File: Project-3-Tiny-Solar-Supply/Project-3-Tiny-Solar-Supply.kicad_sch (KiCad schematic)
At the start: 16 parts, among them J1 Conn_01x02_Pin, J2 Conn_01x02_Pin, J3 Conn_01x02_Pin, J4 Conn_01x02_Pin, Q1 2N7002, U1 AP3015AKTR-G1

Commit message: assign remaining footprints to symbols
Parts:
- C1, C3: footprint (none) -> Capacitor_SMD:C_0805_2012Metric
- C2: footprint (none) -> Capacitor_SMD:C_1206_3216Metric
- J1, J2, J3: footprint (none) -> Connector_PinHeader_2.54mm:PinHeader_1x02_P2.54mm_Vertical
- J4: footprint (none) -> Connector_PinHeader_2.54mm:PinHeader_1x02_P2.54mm_Horizontal
- R1, R2, R3, R4: footprint (none) -> Resistor_SMD:R_0805_2012Metric
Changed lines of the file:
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@@
 			)
 		)
-		(property "Footprint" ""
+		(property "Footprint" "Connector_PinHeader_2.54mm:PinHeader_1x02_P2.54mm_Vertical"
 			(at 86.36 54.61 0)
 			(hide yes)
@@
 			)
 		)
-		(property "Footprint" ""
+		(property "Footprint" "Resistor_SMD:R_0805_2012Metric"
 			(at 116.332 45.72 90)
 			(hide yes)
@@
 			)
 		)
-		(property "Footprint" ""
+		(property "Footprint" "Capacitor_SMD:C_0805_2012Metric"
 			(at 216.8652 52.07 0)
 			(hide yes)
@@
 			)
 		)
-		(property "Footprint" ""
+		(property "Footprint" "Connector_PinHeader_2.54mm:PinHeader_1x02_P2.54mm_Horizontal"
 			(at 53.34 52.07 0)
 			(hide yes)
@@
 			)
 		)
-		(property "Footprint" ""
+		(property "Footprint" "Resistor_SMD:R_0805_2012Metric"
 			(at 62.992 67.31 90)
 			(hide yes)
@@
 			)
 		)
-		(property "Footprint" ""
+		(property "Footprint" "Connector_PinHeader_2.54mm:PinHeader_1x02_P2.54mm_Vertical"
 			(at 104.14 34.29 0)
 			(hide yes)
@@
 			)
 		)
-		(property "Footprint" ""
+		(property "Footprint" "Resistor_SMD:R_0805_2012Metric"
 			(at 198.882 81.28 90)
 			(hide yes)
@@
 			)
 		)
-		(property "Footprint" ""
+		(property "Footprint" "Capacitor_SMD:C_1206_3216Metric"
 			(at 224.4852 69.85 0)
 			(hide yes)
@@
 			)
 		)
-		(property "Footprint" ""
+		(property "Footprint" "Resistor_SMD:R_0805_2012Metric"
 			(at 198.882 48.26 90)
 			(hide yes)
@@
 			)
 		)
-		(property "Footprint" ""
+		(property "Footprint" "Capacitor_SMD:C_0805_2012Metric"
 			(at 135.5852 85.09 0)
 			(hide yes)
@@
 			)
 		)
-		(property "Footprint" ""
+		(property "Footprint" "Connector_PinHeader_2.54mm:PinHeader_1x02_P2.54mm_Vertical"
 			(at 240.03 59.69 0)
 			(hide yes)

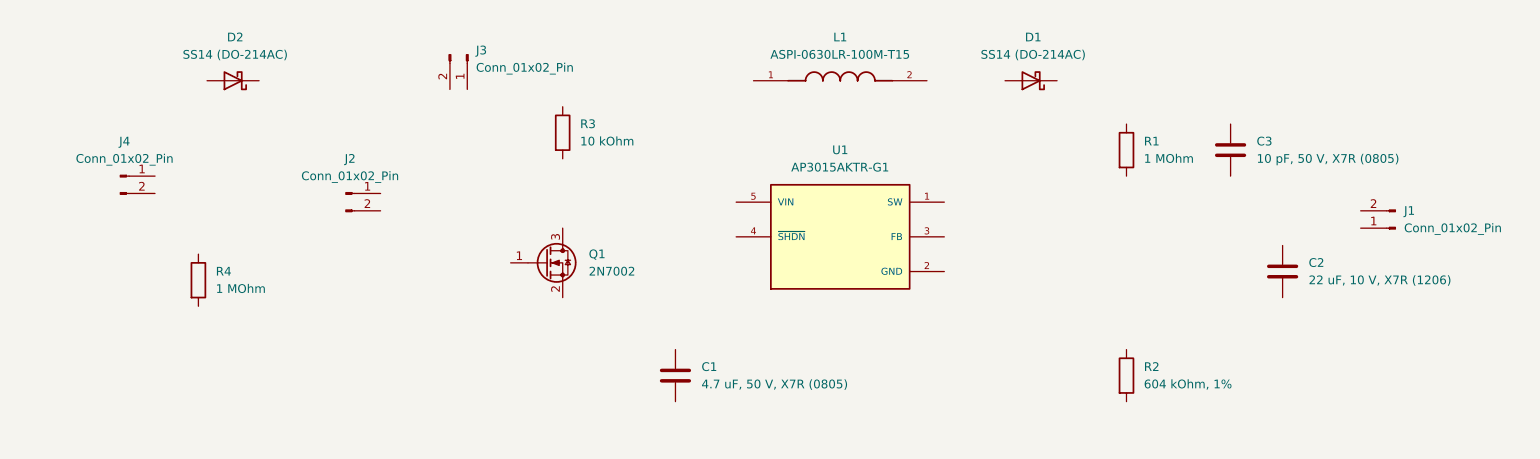
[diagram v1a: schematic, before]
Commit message: wire schematic symbols
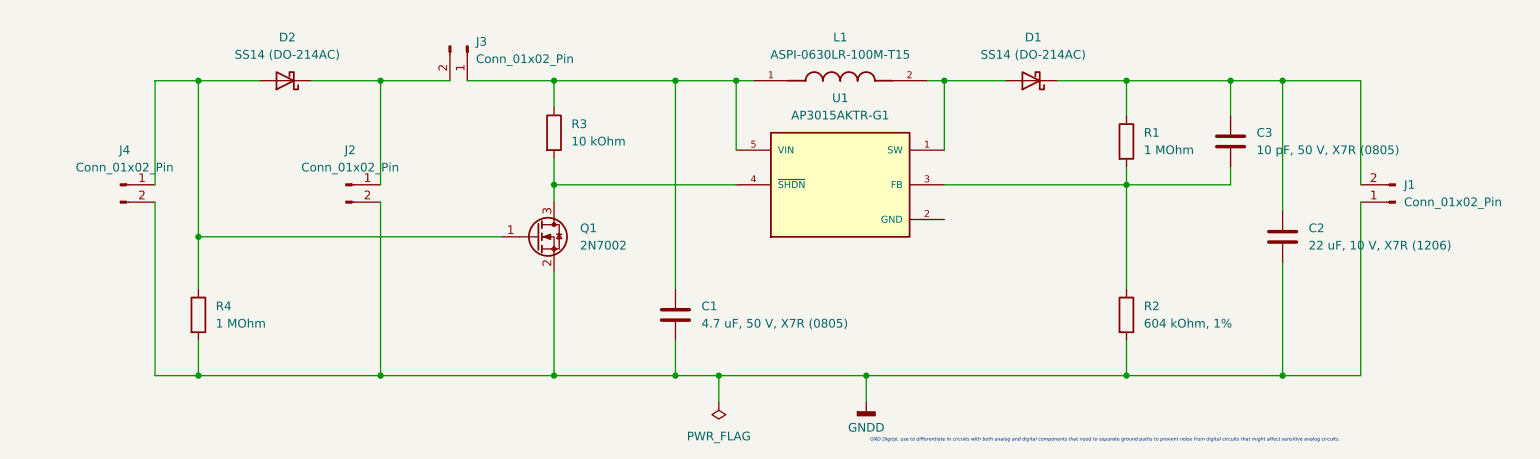
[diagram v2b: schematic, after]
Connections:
- net at J2.1 (Pin_1): now also D2.1 (K), J3.2 (Pin_2)
- net GNDD: now reaches J2.2 (Pin_2)
- net GNDD: now also C1.2, C2.2, J1.1 (Pin_1), J4.2 (Pin_2), Q1.2 (S), R2.2, R4.2
- net at R3.1: now also C1.1, J3.1 (Pin_1), L1.1, U1.5 (VIN)
- net at R3.2: now also Q1.3 (D), U1.4 (~{SHDN})
- net at L1.2: now also D1.2 (A), U1.1 (SW)
- net at C3.1: now also C2.1, D1.1 (K), J1.2 (Pin_2), R1.1
- net at C3.2: now also R1.2, R2.1, U1.3 (FB)
- net at J4.1 (Pin_1): now also D2.2 (A), Q1.1 (G), R4.1
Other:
- note added: "GND Digital, use to differentiate in circuits with both analog and digital components that need to separate ground paths to prevent noise from digital circuits that might affect sensitive analog circuits."
- moved on the sheet: C1, C2, C3, D2, J1, J2, J3, J4, Q1, R1, R2, R3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

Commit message: bugfix missing Voltage Regulator's GND connection, and add net labels
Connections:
- net GNDD: now also U1.2 (GND)
- net BAT_P: now reaches D2.1 (K), J2.1 (Pin_1), J3.2 (Pin_2)
- net OUT_P: now reaches C2.1, C3.1, D1.1 (K), J1.2 (Pin_2), R1.1
- net SOLAR_P: now reaches D2.2 (A), J4.1 (Pin_1), Q1.1 (G), R4.1
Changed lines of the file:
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@@
+	)
+	(junction
+		(at 173.99 81.28)
+		(diameter 0)
+		(color 0 0 0 0)
 	)
 	(junction
@@
 	(wire
 		(pts
+			(xy 173.99 58.42) (xy 173.99 81.28)
+		)
+		(stroke
+			(width 0)
+			(type default)
+		)
+	)
+	(wire
+		(pts
 			(xy 171.45 38.1) (xy 173.99 38.1)
 		)
@@
 	(wire
 		(pts
+			(xy 173.99 81.28) (xy 200.66 81.28)
+		)
+		(stroke
+			(width 0)
+			(type default)
+		)
+	)
+	(wire
+		(pts
 			(xy 140.97 85.09) (xy 140.97 81.28)
 		)
@@
 	(wire
 		(pts
-			(xy 162.56 81.28) (xy 200.66 81.28)
+			(xy 162.56 81.28) (xy 173.99 81.28)
 		)
 		(stroke
@@
 		)
 	)
+	(label "SOLAR_P"
+		(at 58.42 38.1 180)
+		(effects
+			(font
+				(size 1.27 1.27)
+				(italic yes)
+			)
+			(justify right bottom)
+		)
+	)
+	(label "OUT_P"
+		(at 234.95 38.1 0)
+		(effects
+			(font
+				(size 1.27 1.27)
+				(italic yes)
+			)
+			(justify left bottom)
+		)
+	)
+	(label "BAT_P"
+		(at 91.44 44.45 0)
+		(effects
+			(font
+				(size 1.27 1.27)
+				(italic yes)
+			)
+			(justify left bottom)
+		)
+	)

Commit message: add connectors' descriptions
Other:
- note added: "BATTERY"
- note added: "ON/OFF"
- note added: "OUT"
- note added: "SOLAR_IN"
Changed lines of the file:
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@@
 		(rev "1")
+	)
+	(text "SOLAR_IN"
+		(exclude_from_sim no)
+		(at 46.99 53.975 0)
+		(effects
+			(font
+				(size 1.27 1.27)
+				(thickness 0.254)
+				(bold yes)
+			)
+		)
+	)
+	(text "ON/OFF"
+		(exclude_from_sim no)
+		(at 103.505 29.845 0)
+		(effects
+			(font
+				(size 1.27 1.27)
+				(thickness 0.254)
+				(bold yes)
+			)
+		)
 	)
 	(text "GND Digital, use to differentiate in circuits with both analog and digital components that need to separate ground paths to prevent noise from digital circuits that might affect sensitive analog circuits."
@@
 				(size 0.5 0.5)
 				(italic yes)
+			)
+		)
+	)
+	(text "OUT"
+		(exclude_from_sim no)
+		(at 247.65 53.975 0)
+		(effects
+			(font
+				(size 1.27 1.27)
+				(thickness 0.254)
+				(bold yes)
+			)
+		)
+	)
+	(text "BATTERY"
+		(exclude_from_sim no)
+		(at 81.915 55.245 0)
+		(effects
+			(font
+				(size 1.27 1.27)
+				(thickness 0.254)
+				(bold yes)
 			)
 		)
@@
 			)
 		)
+		(property "MPN" ""
+			(at 158.75 38.1 0)
+			(show_name no)
+			(do_not_autoplace no)
+			(effects
+				(font
+					(size 1.27 1.27)
+				)
+			)
+		)
+		(property "Manufacturer" ""
+			(at 158.75 38.1 0)
+			(show_name no)
+			(do_not_autoplace no)
+			(effects
+				(font
+					(size 1.27 1.27)
+				)
+			)
+		)
+		(property "Purpose" ""
+			(at 158.75 38.1 0)
+			(show_name no)
+			(do_not_autoplace no)
+			(effects
+				(font
+					(size 1.27 1.27)
+				)
+			)
+		)

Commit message: remove text boxes and add 'purpose' field value to the connectors
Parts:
- J1: Purpose (none) -> Power output
- J2: Purpose (none) -> Battery connector
- J3: Purpose (none) -> On/Off switch
- J4: Purpose (none) -> Solar connector
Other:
- note removed: "BATTERY"
- note removed: "ON/OFF"
- note removed: "OUT"
- note removed: "SOLAR_IN"
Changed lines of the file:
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@@
 		(rev "1")
-	)
-	(text "SOLAR_IN"
-		(exclude_from_sim no)
-		(at 46.99 53.975 0)
-		(effects
-			(font
-				(size 1.27 1.27)
-				(thickness 0.254)
-				(bold yes)
-			)
-		)
-	)
-	(text "ON/OFF"
-		(exclude_from_sim no)
-		(at 103.505 29.845 0)
-		(effects
-			(font
-				(size 1.27 1.27)
-				(thickness 0.254)
-				(bold yes)
-			)
-		)
 	)
 	(text "GND Digital, use to differentiate in circuits with both analog and digital components that need to separate ground paths to prevent noise from digital circuits that might affect sensitive analog circuits."
@@
 				(size 0.5 0.5)
 				(italic yes)
-			)
-		)
-	)
-	(text "OUT"
-		(exclude_from_sim no)
-		(at 247.65 53.975 0)
-		(effects
-			(font
-				(size 1.27 1.27)
-				(thickness 0.254)
-				(bold yes)
-			)
-		)
-	)
-	(text "BATTERY"
-		(exclude_from_sim no)
-		(at 81.915 55.245 0)
-		(effects
-			(font
-				(size 1.27 1.27)
-				(thickness 0.254)
-				(bold yes)
 			)
 		)
@@
 		(in_pos_files yes)
 		(dnp no)
-		(fields_autoplaced yes)
 		(property "Reference" "J2"
 			(at 86.995 48.26 0)
@@
 			(at 86.36 53.34 0)
 			(hide yes)
+			(show_name no)
+			(do_not_autoplace no)
+			(effects
+				(font
+					(size 1.27 1.27)
+				)
+			)
+		)
+		(property "Purpose" "Battery connector"
+			(at 78.105 54.61 0)
 			(show_name no)
 			(do_not_autoplace no)
@@
 		(in_pos_files yes)
 		(dnp no)
-		(fields_autoplaced yes)
 		(property "Reference" "J4"
 			(at 53.975 48.26 0)
@@
 			(at 53.34 53.34 0)
 			(hide yes)
+			(show_name no)
+			(do_not_autoplace no)
+			(effects
+				(font
+					(size 1.27 1.27)
+				)
+			)
+		)
+		(property "Purpose" "Solar connector"
+			(at 46.99 54.61 0)
 			(show_name no)
 			(do_not_autoplace no)
@@
 		(in_pos_files yes)
 		(dnp no)
-		(fields_autoplaced yes)
 		(property "Reference" "J3"
 			(at 105.41 32.3849 90)
@@
 			(at 104.14 33.02 0)
 			(hide yes)
+			(show_name no)
+			(do_not_autoplace no)
+			(effects
+				(font
+					(size 1.27 1.27)
+				)
+			)
+		)
+		(property "Purpose" "On/Off switch"
+			(at 104.14 31.115 90)
 			(show_name no)
 			(do_not_autoplace no)
@@
 		(in_pos_files yes)
 		(dnp no)
-		(fields_autoplaced yes)
 		(property "Reference" "J1"
 			(at 241.3 53.3399 0)
@@
 			(show_name no)
 			(do_not_autoplace no)
+			(effects
+				(font
+					(size 1.27 1.27)
+				)
+			)
+		)
+		(property "Purpose" "Power output"
+			(at 250.825 53.34 0)
+			(show_name no)
+			(do_not_autoplace no)

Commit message: update associated footprints for J1, J2, J3
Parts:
- J1, J2: footprint Connector_PinHeader_2.54mm:PinHeader_1x02_P2.54mm_Vertical -> Connector_PinHeader_2.54mm:PinHeader_1x02_P2.54mm_Horizontal
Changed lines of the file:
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@@
 			)
 		)
-		(property "Footprint" "Connector_PinHeader_2.54mm:PinHeader_1x02_P2.54mm_Vertical"
+		(property "Footprint" "Connector_PinHeader_2.54mm:PinHeader_1x02_P2.54mm_Horizontal"
 			(at 86.36 53.34 0)
 			(hide yes)
@@
 		(property "Purpose" "Battery connector"
 			(at 78.105 54.61 0)
+			(show_name no)
+			(do_not_autoplace no)
+			(effects
+				(font
+					(size 1.27 1.27)
+				)
+			)
+		)
+		(property "MPN" ""
+			(at 86.36 53.34 0)
+			(show_name no)
+			(do_not_autoplace no)
+			(effects
+				(font
+					(size 1.27 1.27)
+				)
+			)
+		)
+		(property "Manufacturer" ""
+			(at 86.36 53.34 0)
 			(show_name no)
 			(do_not_autoplace no)
@@
 			)
 		)
-		(property "Footprint" "Connector_PinHeader_2.54mm:PinHeader_1x02_P2.54mm_Vertical"
+		(property "Footprint" "Connector_PinHeader_2.54mm:PinHeader_1x02_P2.54mm_Horizontal"
 			(at 240.03 55.88 0)
 			(hide yes)
@@
 			(show_name no)
 			(do_not_autoplace no)
+			(effects
+				(font
+					(size 1.27 1.27)
+				)
+			)
+		)
+		(property "MPN" ""
+			(at 240.03 55.88 0)
+			(show_name no)
+			(do_not_autoplace no)
+			(effects
+				(font
+					(size 1.27 1.27)
+				)
+			)
+		)
+		(property "Manufacturer" ""
+			(at 240.03 55.88 0)
+			(show_name no)
+			(do_not_autoplace no)

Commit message: update associated footprint for J3 (from jumper connector to button switch)
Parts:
- J3: footprint Connector_PinHeader_2.54mm:PinHeader_1x02_P2.54mm_Vertical -> Button_Switch_THT:SW_DIP_SPSTx01_Slide_9.78x4.72mm_W7.62mm_P2.54mm
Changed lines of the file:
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@@
 			)
 		)
-		(property "Footprint" "Connector_PinHeader_2.54mm:PinHeader_1x02_P2.54mm_Vertical"
+		(property "Footprint" "Button_Switch_THT:SW_DIP_SPSTx01_Slide_9.78x4.72mm_W7.62mm_P2.54mm"
 			(at 104.14 33.02 0)
 			(hide yes)
@@
 			(show_name no)
 			(do_not_autoplace no)
+			(effects
+				(font
+					(size 1.27 1.27)
+				)
+			)
+		)
+		(property "MPN" ""
+			(at 104.14 33.02 0)
+			(show_name no)
+			(do_not_autoplace no)
+			(effects
+				(font
+					(size 1.27 1.27)
+				)
+			)
+		)
+		(property "Manufacturer" ""
+			(at 104.14 33.02 0)
+			(show_name no)
+			(do_not_autoplace no)
